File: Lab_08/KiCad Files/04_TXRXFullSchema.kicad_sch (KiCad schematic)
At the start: 60 parts

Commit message: Complete Lab 8 First Revision Schema
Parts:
- removed R? (x2): 10K, symbol Device:R
- added C?: 100pF, symbol Device:C
- added C?: 0.01uF, symbol Device:C
- added C?: 470pF, symbol Device:C
- added C?: 0.001uF, symbol Device:C
- added D? (x2): D, symbol Device:D
- added J?: Banana Jack, symbol Connector:Conn_01x01_Socket
- added Q?: NPN, symbol Simulation_SPICE:NPN
- added Q? (x2): PNP, symbol Simulation_SPICE:PNP
- added R?: 39K, symbol Device:R
- added R?: 1M, symbol Device:R
- added R? (x2): 1K, symbol Device:R
- added R? (x2): 10K, symbol Device:R
- added R?: 100R, symbol Device:R
- added R?: 15K, symbol Device:R
- added RV?: 10K, symbol Device:R_Potentiometer_Trim
- added U? (x3): TL082, symbol Amplifier_Operational:TL082
- C? (x2): value 0.1uF -> 0.01uF
- C?: value 0.047uF -> 0.01uF
- R?: value 100K -> 2K2
- R?: value 100K -> 1K
- R? (x2): value 270R -> 120R
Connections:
- net +15V: now also R?.1, D?.2 (A), Q?.3 (E), R?.1, R?.1, RV?.1, U?.8 (V+)
- net GND: now also U?.3, U?.9, C?.2, C?.2, C?.2, Q?.3 (E), R?.2, U?.4 (V-)
- net RESET: now reaches U?.5, U?.6
- net RESET: now also U?.6 (Q)
- net at U?.4, U?.8: now also U?.1, U?.11, C?.1, Q?.1 (C)
- net CAPTURE: now reaches U?.5 (Clk-), U?.6 (Q)
- net CAPTURE: now also U?.12, U?.13
- net at U?.10, U?.2: now also C?.1, U?.3 (+)
- net at J?.1 (Pin_1), R?.1: now also R?.1
- net at U?.5 (Clk-): now also Q?.1 (C), R?.2, R?.2
- new net: Q?.2 (B), R?.2 (x2)
- new net: D?.1 (K), D?.2 (A)
- new net: C?.2, R?.1, R?.2
- new net: C?.1, R?.2, U?.5 (+)
- new net: Q?.3 (E), R?.2
- new net: C?.1, J?.1 (Pin_1), U?.6 (-), U?.7
- new net: D?.1 (K), Q?.1 (C), RV?.3
- new net: R?.1, RV?.2
- new net: Q?.2 (B), R?.1
- new net: R?.1, U?.1, U?.2 (-)
- new net: R?.1, U?. (VCC)
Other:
- note added: "Filter"
- note added: "Level Shift"
- note added: "OUTPUT"
- note added: "Offset Calibrate"
- note added: "One-Shot"
- note added: "RC = 1% of cycle time"
- note added: "RC = 2% of cycle time"
- note added: "RECEIVER/ DEMODULATOR"
- note added: "Ramp Gen."
- note added: "Receive Module"
- note added: "Sample & Hold"
- note added: "Schmitt Trigger"
- note added: "Transmit Module"
- moved on the sheet: C?, D?, J?, Q?, R?, RV?, U?, U?A, U?B, U?C, U?D, U?E

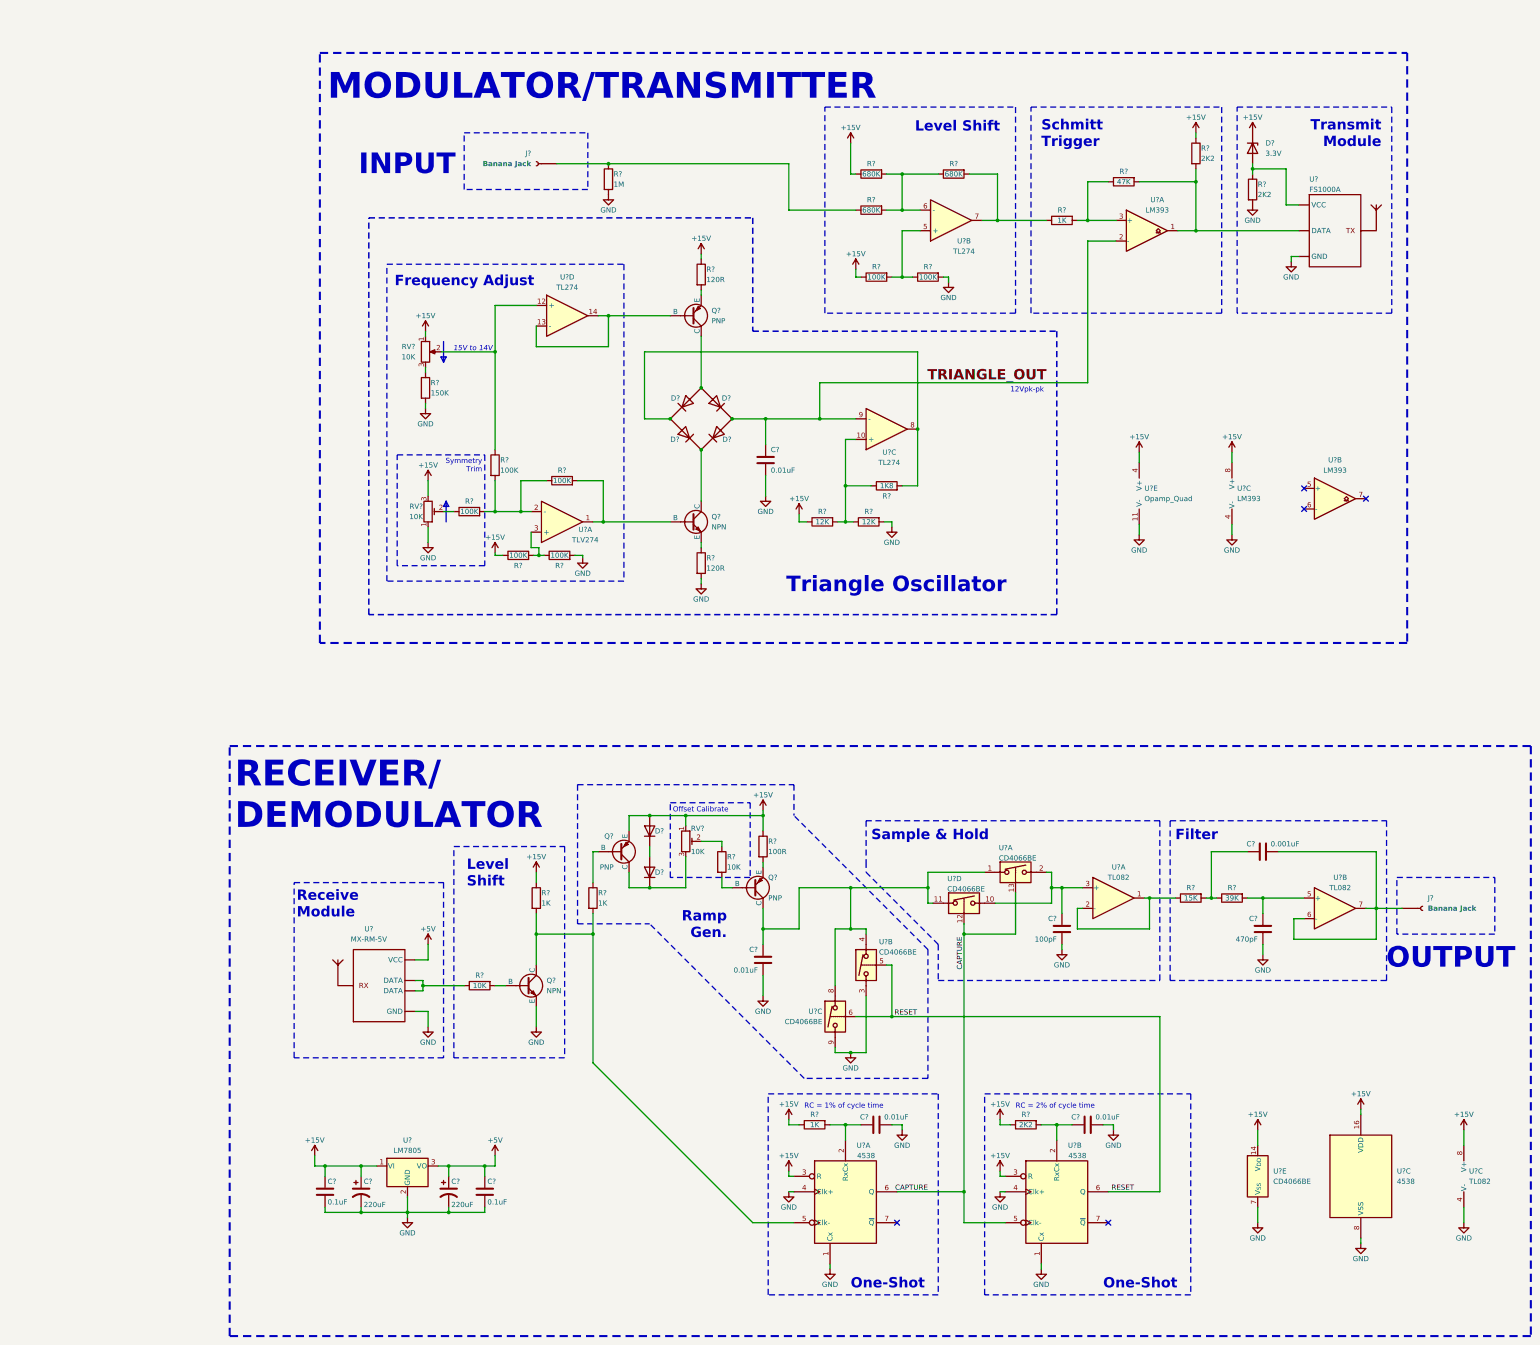
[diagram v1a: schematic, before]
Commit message: Annotate Part 1 Schematic
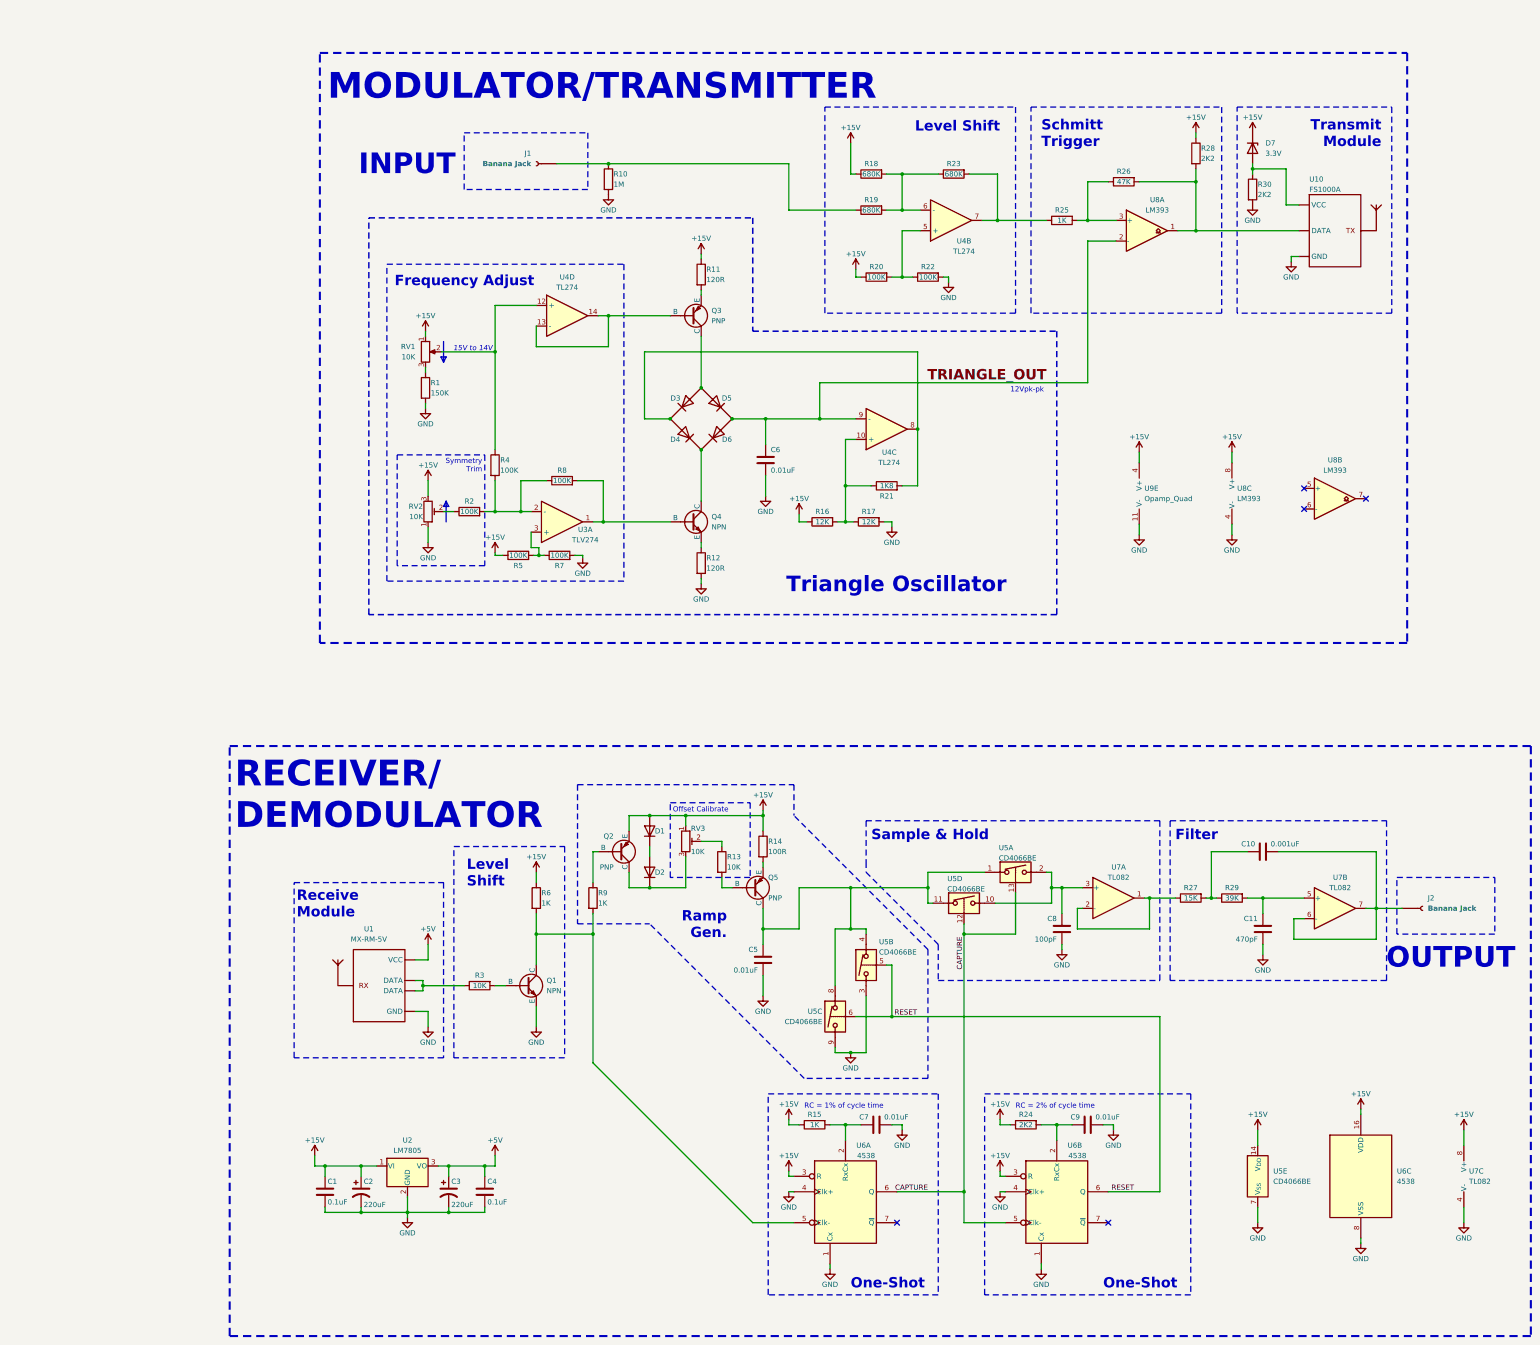
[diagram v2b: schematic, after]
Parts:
- gave numbers to parts that had none: 68

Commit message: Continue Lab 8
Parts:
- removed R7: 100K, symbol Device:R
- added C1, C3: 22uF, Capacitor_THT:CP_Radial_D6.3mm_P2.50mm, symbol Device:C_Polarized_US
- added C4: 0.1uF, Capacitor_THT:C_Rect_L11.0mm_W2.8mm_P10.00mm_MKT, symbol Device:C
- added R5: 100K, Resistor_THT:R_Axial_DIN0207_L6.3mm_D2.5mm_P7.62mm_Horizontal, symbol Device:R
- C101: renamed from C1; footprint (none) -> Capacitor_THT:C_Rect_L11.0mm_W2.8mm_P10.00mm_MKT
- C102: renamed from C2; footprint (none) -> Capacitor_THT:CP_Radial_D8.0mm_P5.00mm
- C103: renamed from C3; footprint (none) -> Capacitor_THT:CP_Radial_D8.0mm_P5.00mm
- C104: renamed from C4; footprint (none) -> Capacitor_THT:C_Rect_L11.0mm_W2.8mm_P10.00mm_MKT
- C105: renamed from C5; footprint (none) -> Capacitor_THT:C_Disc_D3.0mm_W1.6mm_P2.50mm
- C106: renamed from C7; value 0.01uF -> 0.001uF; footprint (none) -> Capacitor_THT:C_Disc_D3.0mm_W1.6mm_P2.50mm
- C107: renamed from C8; value 100pF -> 220pF; footprint (none) -> Capacitor_THT:C_Disc_D3.0mm_W1.6mm_P2.50mm
- C108: renamed from C9; value 0.01uF -> 0.001uF; footprint (none) -> Capacitor_THT:C_Disc_D3.0mm_W1.6mm_P2.50mm
- C109: renamed from C10; footprint (none) -> Capacitor_THT:C_Disc_D3.0mm_W1.6mm_P2.50mm
- C110: renamed from C11; footprint (none) -> Capacitor_THT:C_Disc_D3.0mm_W1.6mm_P2.50mm
- C2: renamed from C6; footprint (none) -> Capacitor_THT:C_Disc_D3.0mm_W1.6mm_P2.50mm
- D1: renamed from D3; footprint (none) -> Diode_THT:D_A-405_P7.62mm_Horizontal
- D101: renamed from D1; footprint (none) -> Diode_THT:D_A-405_P7.62mm_Horizontal
- D102: renamed from D2; footprint (none) -> Diode_THT:D_A-405_P7.62mm_Horizontal
- D2: renamed from D4; footprint (none) -> Diode_THT:D_A-405_P7.62mm_Horizontal
- D3: renamed from D5; footprint (none) -> Diode_THT:D_A-405_P7.62mm_Horizontal
- D4: renamed from D6; footprint (none) -> Diode_THT:D_A-405_P7.62mm_Horizontal
- D5: renamed from D7; value 3.3V -> 12V; footprint (none) -> Diode_THT:D_A-405_P7.62mm_Horizontal
- Q1: renamed from Q3; footprint (none) -> Package_TO_SOT_THT:TO-92_Inline_Wide; symbol Simulation_SPICE:PNP -> Transistor_BJT:2N3906
- Q101: renamed from Q1; footprint (none) -> Package_TO_SOT_THT:TO-92_Inline_Wide; symbol Simulation_SPICE:NPN -> Transistor_BJT:2N3904
- Q102: renamed from Q2; footprint (none) -> Package_TO_SOT_THT:TO-92_Inline_Wide; symbol Simulation_SPICE:PNP -> Transistor_BJT:2N3906
- Q103: renamed from Q5; footprint (none) -> Package_TO_SOT_THT:TO-92_Inline_Wide; symbol Simulation_SPICE:PNP -> Transistor_BJT:2N3906
- Q2: renamed from Q4; footprint (none) -> Package_TO_SOT_THT:TO-92_Inline_Wide; symbol Simulation_SPICE:NPN -> Transistor_BJT:2N3904
- R1: footprint (none) -> Resistor_THT:R_Axial_DIN0207_L6.3mm_D2.5mm_P10.16mm_Horizontal
- R10: renamed from R16; footprint (none) -> Resistor_THT:R_Axial_DIN0207_L6.3mm_D2.5mm_P10.16mm_Horizontal
- R101: renamed from R3; footprint (none) -> Resistor_THT:R_Axial_DIN0207_L6.3mm_D2.5mm_P7.62mm_Horizontal
- R102: renamed from R6; footprint (none) -> Resistor_THT:R_Axial_DIN0207_L6.3mm_D2.5mm_P7.62mm_Horizontal
- R103: renamed from R9; footprint (none) -> Resistor_THT:R_Axial_DIN0207_L6.3mm_D2.5mm_P7.62mm_Horizontal
- R104: renamed from R13; footprint (none) -> Resistor_THT:R_Axial_DIN0207_L6.3mm_D2.5mm_P7.62mm_Horizontal
- R105: renamed from R14; footprint (none) -> Resistor_THT:R_Axial_DIN0207_L6.3mm_D2.5mm_P7.62mm_Horizontal
- R106: renamed from R15; value 1K -> 470R; footprint (none) -> Resistor_THT:R_Axial_DIN0207_L6.3mm_D2.5mm_P7.62mm_Horizontal
- R107: renamed from R24; value 2K2 -> 470R; footprint (none) -> Resistor_THT:R_Axial_DIN0207_L6.3mm_D2.5mm_P10.16mm_Horizontal
- R108: renamed from R27; footprint (none) -> Resistor_THT:R_Axial_DIN0207_L6.3mm_D2.5mm_P7.62mm_Horizontal
- R109: renamed from R29; footprint (none) -> Resistor_THT:R_Axial_DIN0207_L6.3mm_D2.5mm_P7.62mm_Horizontal
- R11: renamed from R20; footprint (none) -> Resistor_THT:R_Axial_DIN0207_L6.3mm_D2.5mm_P7.62mm_Horizontal
- R12: renamed from R18; footprint (none) -> Resistor_THT:R_Axial_DIN0207_L6.3mm_D2.5mm_P7.62mm_Horizontal
- R13: renamed from R19; footprint (none) -> Resistor_THT:R_Axial_DIN0207_L6.3mm_D2.5mm_P7.62mm_Horizontal
- R14: renamed from R17; footprint (none) -> Resistor_THT:R_Axial_DIN0207_L6.3mm_D2.5mm_P10.16mm_Horizontal
- R15: renamed from R21; footprint (none) -> Resistor_THT:R_Axial_DIN0207_L6.3mm_D2.5mm_P5.08mm_Vertical
- R16: renamed from R22; footprint (none) -> Resistor_THT:R_Axial_DIN0207_L6.3mm_D2.5mm_P10.16mm_Horizontal
- R17: renamed from R23; footprint (none) -> Resistor_THT:R_Axial_DIN0207_L6.3mm_D2.5mm_P2.54mm_Vertical
- R18: renamed from R25; footprint (none) -> Resistor_THT:R_Axial_DIN0207_L6.3mm_D2.5mm_P7.62mm_Horizontal
- R19: renamed from R26; footprint (none) -> Resistor_THT:R_Axial_DIN0207_L6.3mm_D2.5mm_P5.08mm_Vertical
- R2: footprint (none) -> Resistor_THT:R_Axial_DIN0207_L6.3mm_D2.5mm_P7.62mm_Horizontal
- R20: renamed from R28; footprint (none) -> Resistor_THT:R_Axial_DIN0207_L6.3mm_D2.5mm_P7.62mm_Horizontal
- R21: renamed from R30; value 2K2 -> 100R; footprint (none) -> Resistor_THT:R_Axial_DIN0207_L6.3mm_D2.5mm_P7.62mm_Horizontal
- R3: renamed from R4; footprint (none) -> Resistor_THT:R_Axial_DIN0207_L6.3mm_D2.5mm_P10.16mm_Horizontal
- R4: renamed from R5; footprint (none) -> Resistor_THT:R_Axial_DIN0207_L6.3mm_D2.5mm_P10.16mm_Horizontal
- R6: renamed from R8; footprint (none) -> Resistor_THT:R_Axial_DIN0207_L6.3mm_D2.5mm_P5.08mm_Vertical
- R7: renamed from R10; footprint (none) -> Resistor_THT:R_Axial_DIN0207_L6.3mm_D2.5mm_P10.16mm_Horizontal
- R8: renamed from R11; footprint (none) -> Resistor_THT:R_Axial_DIN0207_L6.3mm_D2.5mm_P7.62mm_Horizontal
- R9: renamed from R12; footprint (none) -> Resistor_THT:R_Axial_DIN0207_L6.3mm_D2.5mm_P7.62mm_Horizontal
- RV1, RV2: footprint (none) -> Potentiometer_THT:Potentiometer_ACP_CA9-V10_Vertical
- RV101: renamed from RV3; footprint (none) -> Potentiometer_THT:Potentiometer_ACP_CA9-V10_Vertical
- U1: renamed from U4; value TL274 -> TLV274I; footprint (none) -> Package_DIP:DIP-14_W7.62mm
- U1: renamed from U3; value TLV274 -> TLV274I; footprint (none) -> Package_DIP:DIP-14_W7.62mm
- U1: renamed from U9; value Opamp_Quad -> TLV274I; footprint (none) -> Package_DIP:DIP-14_W7.62mm
- U101: renamed from U1; footprint (none) -> Connector_PinHeader_2.54mm:PinHeader_1x04_P2.54mm_Vertical
- U104: renamed from U6; value 4538 -> CD14538BE; footprint (none) -> Package_DIP:DIP-16_W7.62mm
- U105: renamed from U7; value TL082 -> TL082CN; footprint (none) -> Package_DIP:DIP-8_W7.62mm
- U2: renamed from U8; footprint (none) -> Package_DIP:DIP-8_W7.62mm
- U3: renamed from U10; footprint (none) -> Connector_PinHeader_2.54mm:PinHeader_1x03_P2.54mm_Vertical
- renumbered J2 to J101, U2 to U102, U5 to U103
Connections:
- net +15V: now also Q102.1 (E), R21.1, U104.13 (R); no longer D5.1 (K), Q102.3 (E), U104.3 (R)
- net +5V: now also U101.1 (VCC); no longer U101. (VCC)
- net CAPTURE: now also U104.11 (Clk-); no longer U104.5 (Clk-)
- net GND: now also D5.2 (A), Q101.1 (E), U101.4 (GND), U104.12 (Clk+), U104.15 (Cx), U3.3 (GND), C1.2, C3.2, C4.2, R5.2; no longer Q101.3 (E), R21.2, U101. (VCC), U104.1 (Cx), U104.4 (Clk+), U3. (VCC)
- net RESET: now also U104.10 (Q); no longer U104.6 (Q)
- net at R102.2, R103.2, U104.5 (Clk-): now also Q101.3 (C); no longer Q101.1 (C)
- net at D1.2 (A), D3.2 (A): now also Q1.3 (C); no longer Q1.1 (C)
- net at R19.2, R20.2, U2.1: now also U3.1 (DATA); no longer U3. (VCC)
- net at C105.1, U103.1, U103.11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: now also Q103.3 (C); no longer Q103.1 (C)
- net at R105.2: now also Q103.1 (E); no longer Q103.3 (E)
- net at R3.1, RV1.2: now also U1.3 (+); no longer U1.12 (+)
- net at D2.1 (K), D4.1 (K): now also Q2.3 (C); no longer Q2.1 (C)
- net at R4.2: now also U1.12 (+), C1.1, R5.1; no longer U1.3 (+)
- net at D102.1 (K), RV101.3: now also Q102.3 (C); no longer Q102.1 (C)
- net at C108.2, R107.2: now also U104.14 (RxCx); no longer U104.2 (RxCx)
- net at R11.2, R16.1, U1.5 (+): now also C3.1
- net at R2.2, R3.2, R6.1: now also U1.13 (-); no longer U1.2 (-)
- net at Q2.2 (B), R6.2: now also U1.14; no longer U1.1
- net at R9.1: now also Q2.1 (E); no longer Q2.3 (E)
- net at R101.1: now also U101.2 (DATA), U101.3 (DATA); no longer U101. (VCC)
- net at R8.2: now also Q1.1 (E); no longer Q1.3 (E)
- new net: C4.1, D5.1 (K), R21.2, U3.2 (VCC)
- new net: Q1.2 (B), U1.1, U1.2 (-)
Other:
- note added: "RC = 0.5% of cycle time"
- note removed: "RC = 1% of cycle time"
- note removed: "RC = 2% of cycle time"
- moved on the sheet: D5, J1, R11, R12, R13, R16, R17, R18, R19, R20, R21, R4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
